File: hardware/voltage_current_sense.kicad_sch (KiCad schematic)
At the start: 39 parts, among them U13 INA126U/2K5, U15 MCP6004, U16 LTC6992CS6-2-TRMPBF, U17 6N137, U18 NME0505SC, U8 MCP6004

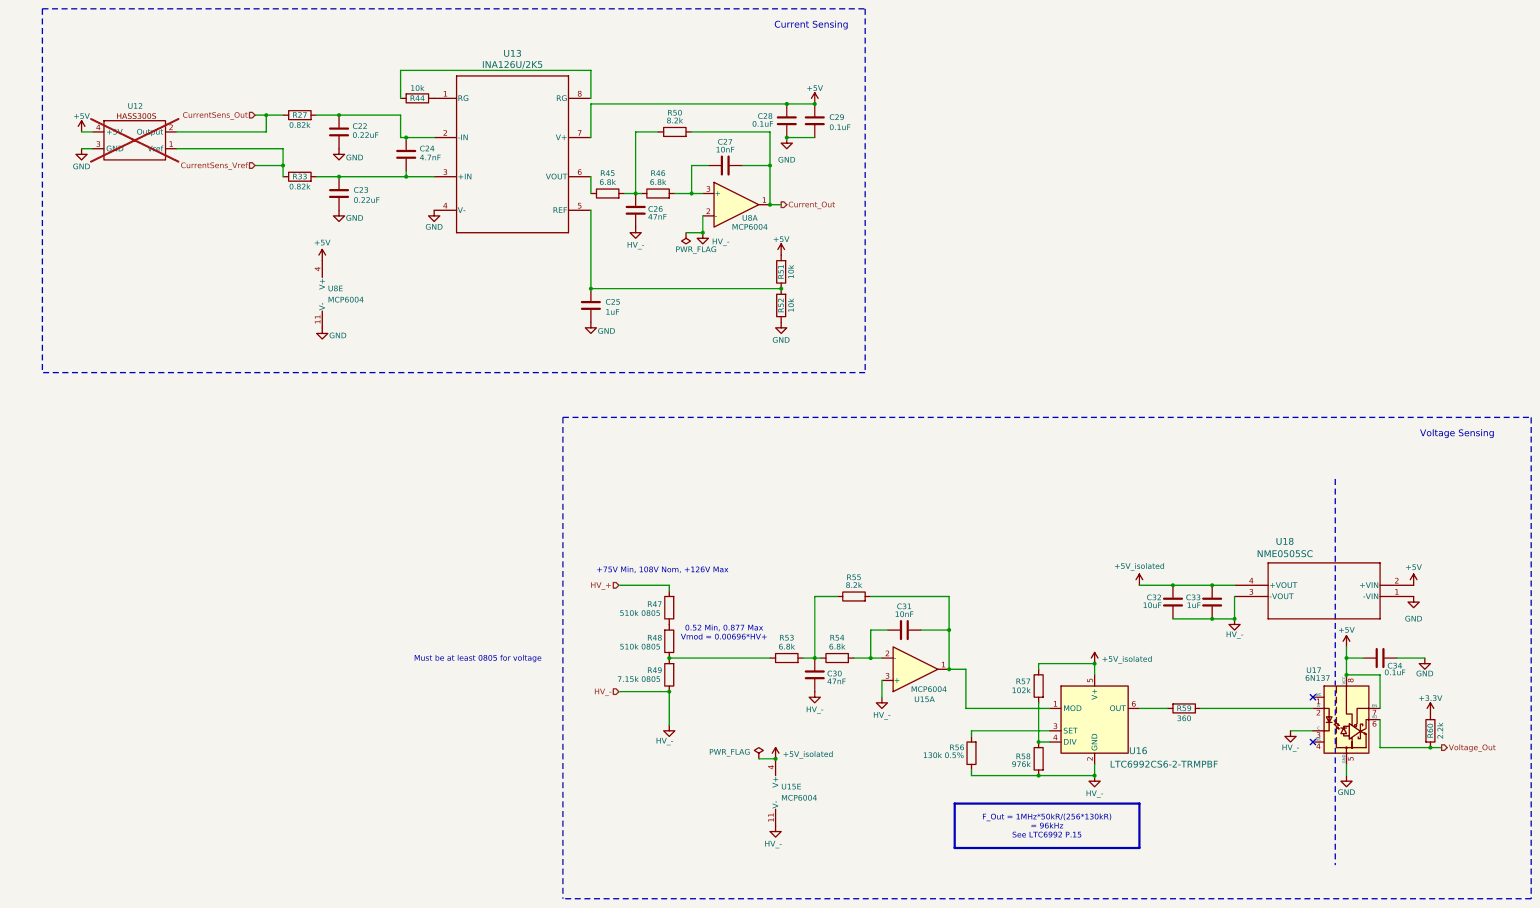
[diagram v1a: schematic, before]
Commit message: initial layout, power traces remain
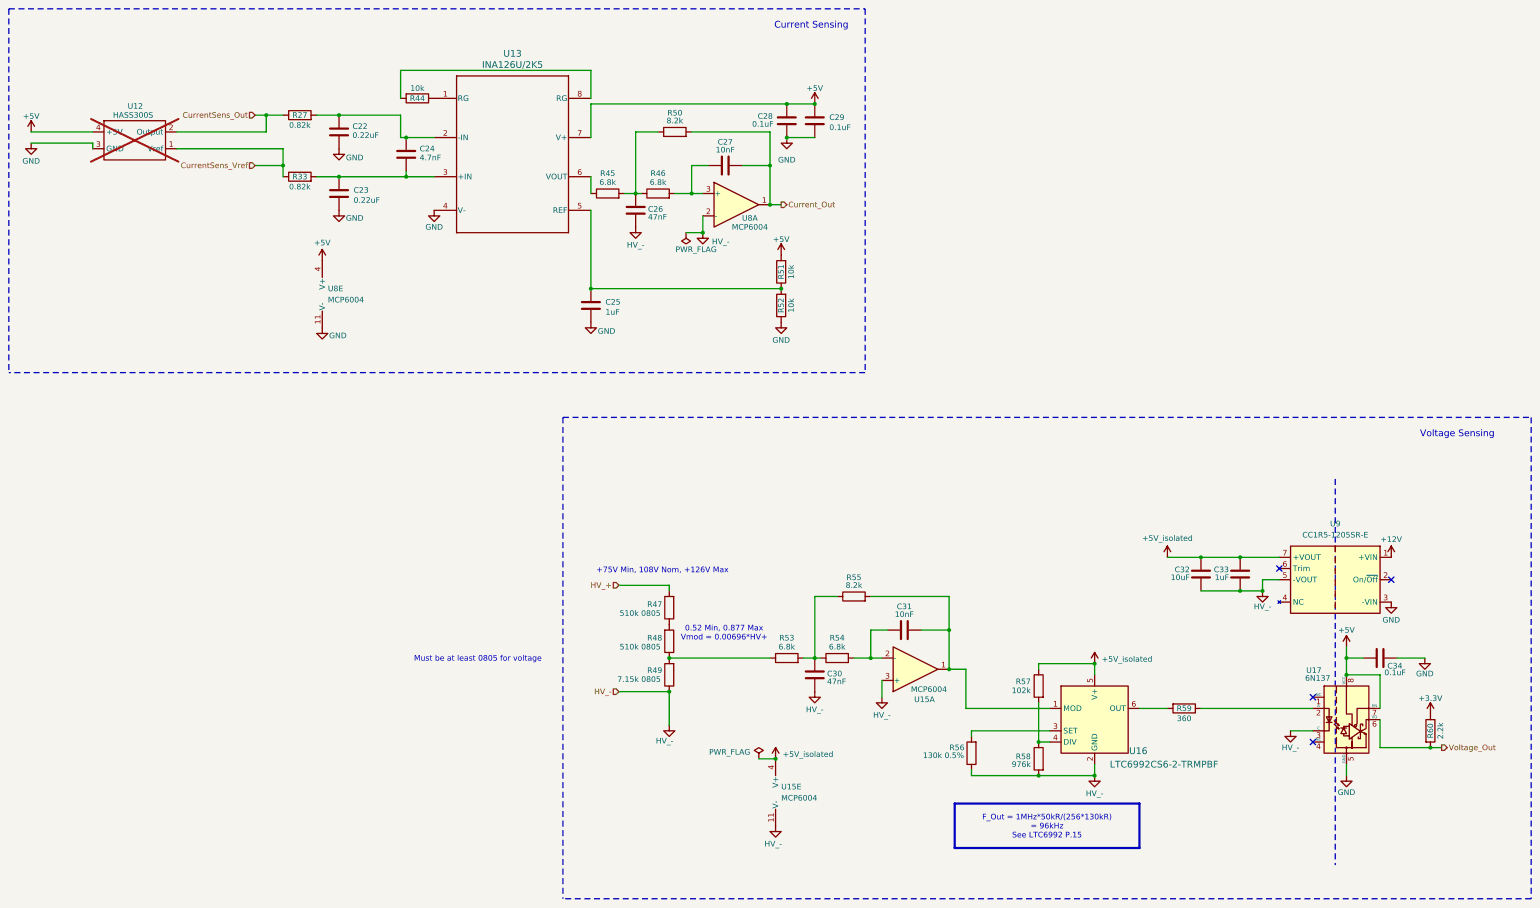
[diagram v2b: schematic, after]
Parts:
- removed U18: NME0505SC, SIP04_NME_11P53X6P1_MUR, symbol NME0505SC:NME0505SC
- added U9: CC1R5-1205SR-E, discharger:CC1R5-1205SR-E, symbol Converter_DCDC:JTD1524S3V3
- U12: value (none) -> HASS300S
- U8: footprint (none) -> Package_SO:SOIC-14_3.9x8.7mm_P1.27mm
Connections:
- net +5V_isolated: now also U9.7 (+VOUT)
- net GND: now also U9.3 (-VIN)
- net HV_-: now also U9.5 (-VOUT)
- new net +12V: U9.1 (+VIN)
- no-connect marks 2 -> 4
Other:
- moved on the sheet: C32, C33
